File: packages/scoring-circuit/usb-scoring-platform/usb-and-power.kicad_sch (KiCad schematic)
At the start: 20 parts, among them J1 GCT USB4105-GF-A, U3 USBLC6-2SC6, U4 AP2112K-3.3TRG1, U5 Adafruit 5807 - set 20V, U6 D36V50F5, U7 AP63203WU-7

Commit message: feat(scoring-circuit): isolate computer USB in native KiCad draft
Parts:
- removed D1: SS14, Diode_SMD:D_SMA, symbol Diode:SS14
- removed R3, R4: 100k 1%, Resistor_SMD:R_0603_1608Metric, symbol Device:R
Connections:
- net GND: no longer C1.2, J1.A1 (GND), J1.A12 (GND), J1.B1 (GND), J1.B12 (GND), J1.SH (SHIELD), R1.2, R2.2, U3.2 (GND)
- net USB_DM renamed USB_HOST_DM
- net USB_DP renamed USB_HOST_DP
- new net USB_GND: C1.2, J1.A1 (GND), J1.A12 (GND), J1.B1 (GND), J1.B12 (GND), J1.SH (SHIELD), R1.2, R2.2, U3.2 (GND)
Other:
- note added: "Computer VBUS supplies only U3 and the upstream USB isolator. No direct USB-to-CORE power path or VBUS divider crosses the barrier."
- note added: "PD powers this revision. USB data is isolated on its own sheet. USB-only acquisition remains open: do not bridge USB_GND/VBUS into the board supply."
- note removed: "Computer USB powers acquisition only. Display, Ethernet and ESP32 require PD. Common-ground engineering draft; NOT an isolated fencing interface."

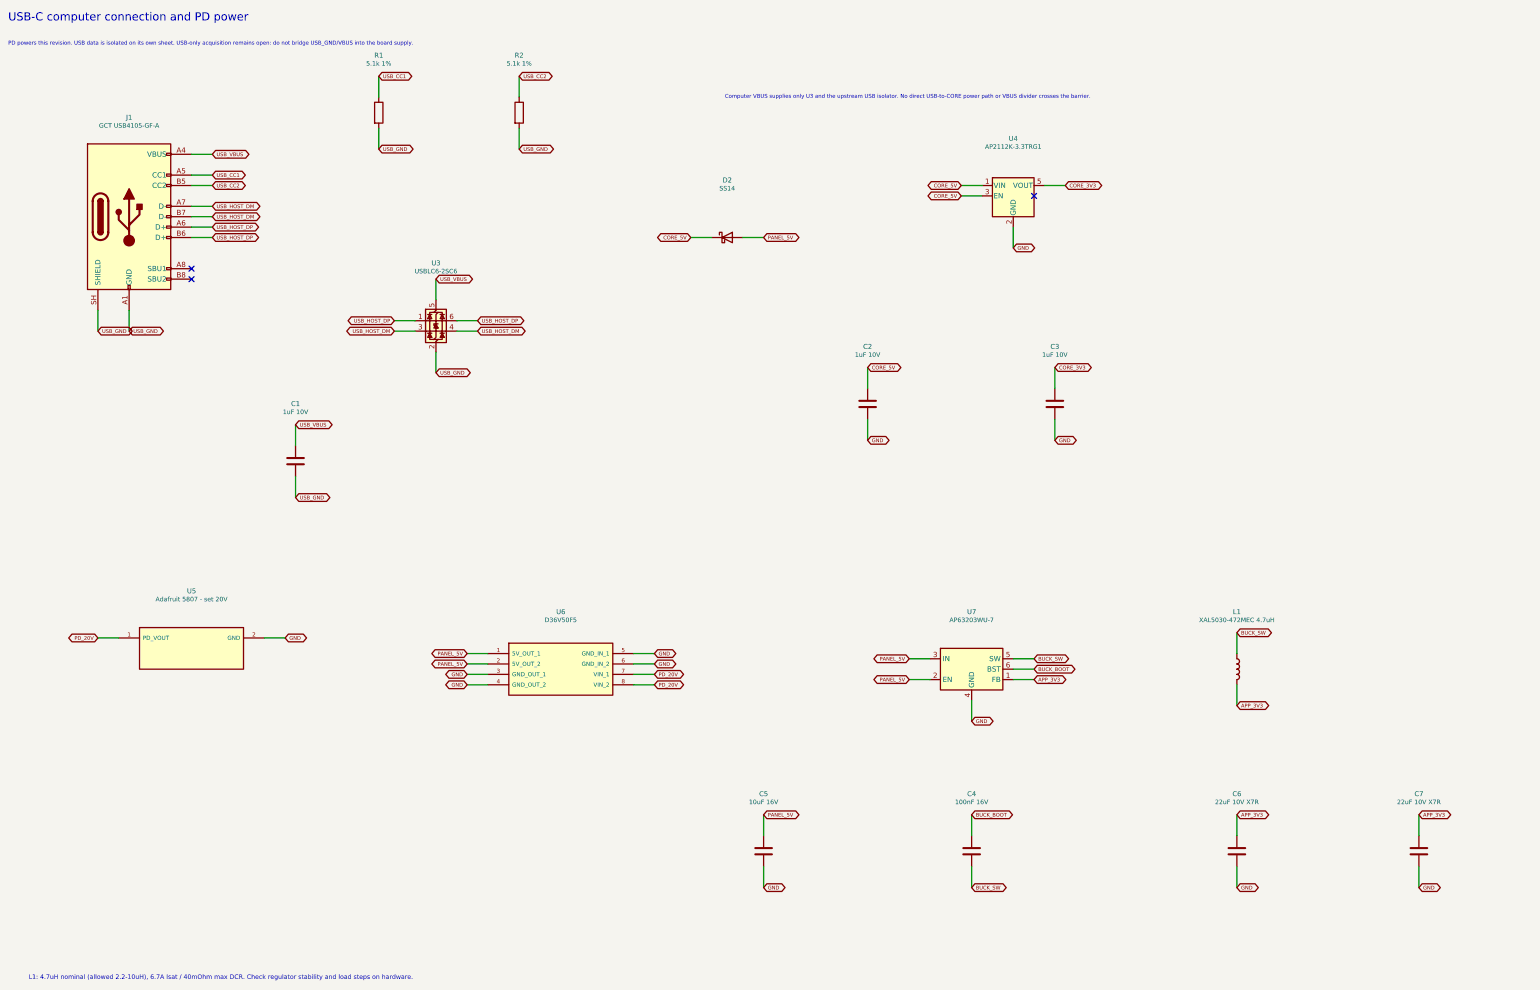
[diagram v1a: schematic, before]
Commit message: feat(scoring-circuit): add isolated single-cable USB acquisition power
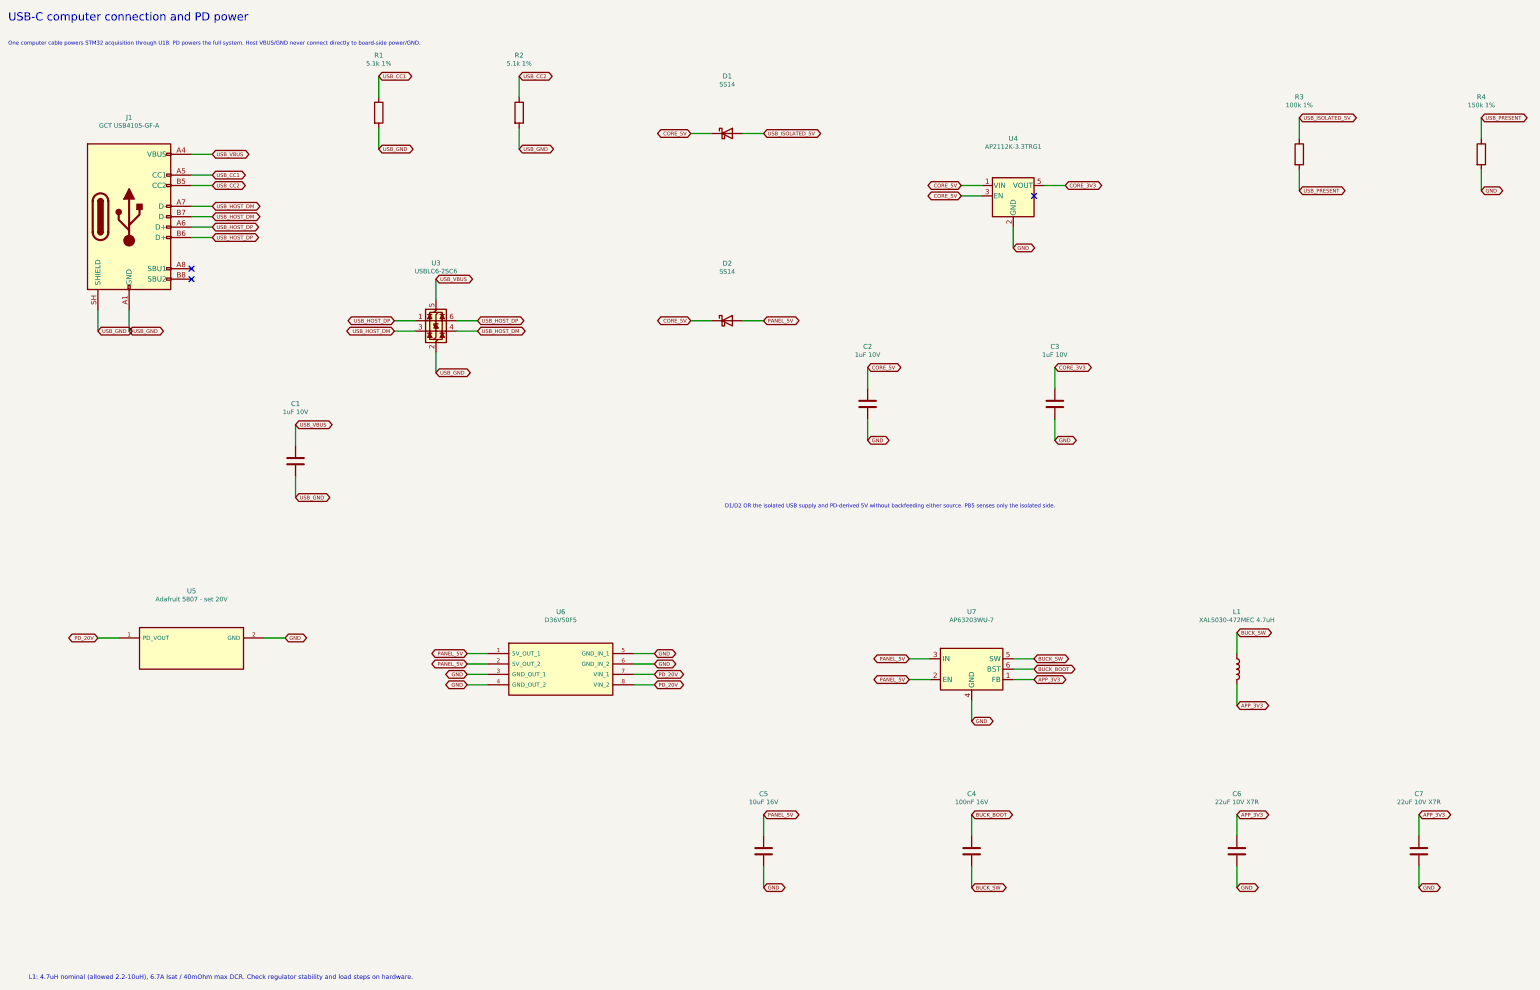
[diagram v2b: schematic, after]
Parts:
- added D1: SS14, Diode_SMD:D_SMA, symbol Diode:SS14
- added R3: 100k 1%, Resistor_SMD:R_0603_1608Metric, symbol Device:R
- added R4: 150k 1%, Resistor_SMD:R_0603_1608Metric, symbol Device:R
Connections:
- net CORE_5V: now also D1.1 (K)
- net GND: now also R4.2
- new net USB_ISOLATED_5V: D1.2 (A), R3.1
- new net USB_PRESENT: R3.2, R4.1
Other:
- note added: "D1/D2 OR the isolated USB supply and PD-derived 5V without backfeeding either source. PB5 senses only the isolated side."
- note added: "One computer cable powers STM32 acquisition through U18. PD powers the full system. Host VBUS/GND never connect directly to board-side power/GND."
- note removed: "Computer VBUS supplies only U3 and the upstream USB isolator. No direct USB-to-CORE power path or VBUS divider crosses the barrier."
- note removed: "PD powers this revision. USB data is isolated on its own sheet. USB-only acquisition remains open: do not bridge USB_GND/VBUS into the board supply."
- moved on the sheet: D2

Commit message: feat(scoring-circuit): decouple USB data protection from VBUS
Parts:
- C1: value 1uF 10V -> 1uF 50V
- U3: value USBLC6-2SC6 -> TPD2E2U06DCKR; footprint Package_TO_SOT_SMD:SOT-23-6 -> ScoringPlatform:TPD2E2U06DCKR; symbol Power_Protection:USBLC6-2SC6 -> Power_Protection:TPD2E2U06DCK
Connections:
- net USB_GND: now also U3.3; no longer U3.2 (GND)
- net USB_HOST_DM: now also U3.2; no longer U3.3 (I/O2), U3.4 (I/O2)
- net USB_HOST_DP: no longer U3.6 (I/O1)
- net USB_VBUS: no longer U3.5 (VBUS)
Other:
- note added: "U3: supply-independent D+/D- protection; no VBUS clamp pin. C1: 50V rating for planned shared PD input. U18 still requires protected input <=16.5V; shared USB-C power conversion remains unfinished."

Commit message: feat(scoring-circuit): replace dual USB inputs with shared isolated power design
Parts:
- removed R1, R2: 5.1k 1%, Resistor_SMD:R_0603_1608Metric, symbol Device:R
- removed U5: Adafruit 5807 - set 20V, ScoringPlatform:Adafruit_5807, symbol ScoringPlatform:Adafruit_5807
- removed U6: D36V50F5, ScoringPlatform:Pololu_D36V50F5, symbol ScoringPlatform:Pololu_D36V50F5
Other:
- note added: "J1 is the only USB-C receptacle. Shared power conversion and PD control are on usb-pd-power. D+/D- remain isolated by U18."
- note removed: "U3: supply-independent D+/D- protection; no VBUS clamp pin. C1: 50V rating for planned shared PD input. U18 still requires protected input <=16.5V; shared USB-C power conversion remains unfinished."
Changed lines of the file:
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@@
 (wire (pts (xy 41.91 87.63) (xy 41.91 92.71)) (stroke (width 0) (type default)))
 (global_label "USB_GND" (shape bidirectional) (at 41.91 92.71 0) (effects (font (size 0.9 0.9)) (justify left)) (property "Intersheetrefs" "" (at 41.91 92.71 0) (effects (font (size 1 1)) (hide yes))))
-(symbol (lib_id "Device:R") (at 110.49 39.37 0) (unit 1) (in_bom yes) (on_board yes) (dnp no) (property "Reference" "R1" (at 110.49 25.37 0) (effects (font (size 1.2 1.2)))) (property "Value" "5.1k 1%" (at 110.49 27.37 0) (effects (font (size 1.1 1.1)))) (property "Footprint" "Resistor_SMD:R_0603_1608Metric" (at 110.49 39.37 0) (effects (font (size 1 1)) (hide yes))) (pin "1") (pin "2") (instances (project "usb-scoring-platform" (path "/20cc8167-128c-446a-a106-f942323e143f/36d13c9b-c278-4925-a3f2-4480b5a41043" (reference "R1") (unit 1)))))
-(wire (pts (xy 110.49 35.56) (xy 110.49 30.48)) (stroke (width 0) (type default)))
-(global_label "USB_CC1" (shape bidirectional) (at 110.49 30.48 0) (effects (font (size 0.9 0.9)) (justify left)) (property "Intersheetrefs" "" (at 110.49 30.48 0) (effects (font (size 1 1)) (hide yes))))
-(wire (pts (xy 110.49 43.18) (xy 110.49 48.26)) (stroke (width 0) (type default)))
-(global_label "USB_GND" (shape bidirectional) (at 110.49 48.26 0) (effects (font (size 0.9 0.9)) (justify left)) (property "Intersheetrefs" "" (at 110.49 48.26 0) (effects (font (size 1 1)) (hide yes))))
-(symbol (lib_id "Device:R") (at 144.78 39.37 0) (unit 1) (in_bom yes) (on_board yes) (dnp no) (property "Reference" "R2" (at 144.78 25.37 0) (effects (font (size 1.2 1.2)))) (property "Value" "5.1k 1%" (at 144.78 27.37 0) (effects (font (size 1.1 1.1)))) (property "Footprint" "Resistor_SMD:R_0603_1608Metric" (at 144.78 39.37 0) (effects (font (size 1 1)) (hide yes))) (pin "1") (pin "2") (instances (project "usb-scoring-platform" (path "/20cc8167-128c-446a-a106-f942323e143f/36d13c9b-c278-4925-a3f2-4480b5a41043" (reference "R2") (unit 1)))))
-(wire (pts (xy 144.78 35.56) (xy 144.78 30.48)) (stroke (width 0) (type default)))
-(global_label "USB_CC2" (shape bidirectional) (at 144.78 30.48 0) (effects (font (size 0.9 0.9)) (justify left)) (property "Intersheetrefs" "" (at 144.78 30.48 0) (effects (font (size 1 1)) (hide yes))))
-(wire (pts (xy 144.78 43.18) (xy 144.78 48.26)) (stroke (width 0) (type default)))
-(global_label "USB_GND" (shape bidirectional) (at 144.78 48.26 0) (effects (font (size 0.9 0.9)) (justify left)) (property "Intersheetrefs" "" (at 144.78 48.26 0) (effects (font (size 1 1)) (hide yes))))
 (symbol (lib_id "Power_Protection:TPD2E2U06DCK") (at 124.46 90.17 0) (unit 1) (in_bom yes) (on_board yes) (dnp no) (property "Reference" "U3" (at 124.46 76.09 0) (effects (font (size 1.2 1.2)))) (property "Value" "TPD2E2U06DCKR" (at 124.46 78.09 0) (effects (font (size 1.1 1.1)))) (property "Footprint" "ScoringPlatform:TPD2E2U06DCKR" (at 124.46 90.17 0) (effects (font (size 1 1)) (hide yes))) (instances (project "usb-scoring-platform" (path "/20cc8167-128c-446a-a106-f942323e143f/36d13c9b-c278-4925-a3f2-4480b5a41043" (reference "U3") (unit 1)))) (property "Datasheet" "https://www.ti.com/lit/ds/symlink/tpd2e2u06.pdf" (at 124.46 90.17 0) (effects (font (size 1 1)) (hide yes))) (pin "1") (pin "2") (pin "3"))
 (symbol (lib_id "Device:C") (at 90.17 124.46 0) (unit 1) (in_bom yes) (on_board yes) (dnp no) (property "Reference" "C1" (at 90.17 110.46 0) (effects (font (size 1.2 1.2)))) (property "Value" "1uF 50V" (at 90.17 112.46 0) (effects (font (size 1.1 1.1)))) (property "Footprint" "Capacitor_SMD:C_0603_1608Metric" (at 90.17 124.46 0) (effects (font (size 1 1)) (hide yes))) (pin "1") (pin "2") (instances (project "usb-scoring-platform" (path "/20cc8167-128c-446a-a106-f942323e143f/36d13c9b-c278-4925-a3f2-4480b5a41043" (reference "C1") (unit 1)))))
@@
 (global_label "GND" (shape bidirectional) (at 379.73 58.42 0) (effects (font (size 0.9 0.9)) (justify left)) (property "Intersheetrefs" "" (at 379.73 58.42 0) (effects (font (size 1 1)) (hide yes))))
 (text "D1/D2 OR the isolated USB supply and PD-derived 5V without backfeeding either source. PB5 senses only the isolated side." (at 195 135 0) (effects (font (size 0.95 0.95)) (justify left top)))
-(symbol (lib_id "ScoringPlatform:Adafruit_5807") (at 64.77 170.18 0) (unit 1) (in_bom yes) (on_board yes) (dnp no) (property "Reference" "U5" (at 64.77 156.18 0) (effects (font (size 1.2 1.2)))) (property "Value" "Adafruit 5807 - set 20V" (at 64.77 158.18 0) (effects (font (size 1.1 1.1)))) (property "Footprint" "ScoringPlatform:Adafruit_5807" (at 64.77 170.18 0) (effects (font (size 1 1)) (hide yes))) (pin "1") (pin "2") (instances (project "usb-scoring-platform" (path "/20cc8167-128c-446a-a106-f942323e143f/36d13c9b-c278-4925-a3f2-4480b5a41043" (reference "U5") (unit 1)))))
-(wire (pts (xy 46.99 167.64) (xy 41.91 167.64)) (stroke (width 0) (type default)))
-(global_label "PD_20V" (shape bidirectional) (at 41.91 167.64 180) (effects (font (size 0.9 0.9)) (justify right)) (property "Intersheetrefs" "" (at 41.91 167.64 180) (effects (font (size 1 1)) (hide yes))))
-(wire (pts (xy 82.55 167.64) (xy 87.63 167.64)) (stroke (width 0) (type default)))
-(global_label "GND" (shape bidirectional) (at 87.63 167.64 0) (effects (font (size 0.9 0.9)) (justify left)) (property "Intersheetrefs" "" (at 87.63 167.64 0) (effects (font (size 1 1)) (hide yes))))
-(symbol (lib_id "ScoringPlatform:Pololu_D36V50F5") (at 154.94 175.26 0) (unit 1) (in_bom yes) (on_board yes) (dnp no) (property "Reference" "U6" (at 154.94 161.26 0) (effects (font (size 1.2 1.2)))) (property "Value" "D36V50F5" (at 154.94 163.26 0) (effects (font (size 1.1 1.1)))) (property "Footprint" "ScoringPlatform:Pololu_D36V50F5" (at 154.94 175.26 0) (effects (font (size 1 1)) (hide yes))) (pin "1") (pin "2") (pin "3") (pin "4") (pin "5") (pin "6") (pin "7") (pin "8") (instances (project "usb-scoring-platform" (path "/20cc8167-128c-446a-a106-f942323e143f/36d13c9b-c278-4925-a3f2-4480b5a41043" (reference "U6") (unit 1)))))
-(wire (pts (xy 137.16 171.45) (xy 132.08 171.45)) (stroke (width 0) (type default)))
-(global_label "PANEL_5V" (shape bidirectional) (at 132.08 171.45 180) (effects (font (size 0.9 0.9)) (justify right)) (property "Intersheetrefs" "" (at 132.08 171.45 180) (effects (font (size 1 1)) (hide yes))))
-(wire (pts (xy 137.16 173.99) (xy 132.08 173.99)) (stroke (width 0) (type default)))
-(global_label "PANEL_5V" (shape bidirectional) (at 132.08 173.99 180) (effects (font (size 0.9 0.9)) (justify right)) (property "Intersheetrefs" "" (at 132.08 173.99 180) (effects (font (size 1 1)) (hide yes))))
-(wire (pts (xy 137.16 176.53) (xy 132.08 176.53)) (stroke (width 0) (type default)))
-(global_label "GND" (shape bidirectional) (at 132.08 176.53 180) (effects (font (size 0.9 0.9)) (justify right)) (property "Intersheetrefs" "" (at 132.08 176.53 180) (effects (font (size 1 1)) (hide yes))))
-(wire (pts (xy 137.16 179.07) (xy 132.08 179.07)) (stroke (width 0) (type default)))
-(global_label "GND" (shape bidirectional) (at 132.08 179.07 180) (effects (font (size 0.9 0.9)) (justify right)) (property "Intersheetrefs" "" (at 132.08 179.07 180) (effects (font (size 1 1)) (hide yes))))
-(wire (pts (xy 172.72 171.45) (xy 177.8 171.45)) (stroke (width 0) (type default)))
-(global_label "GND" (shape bidirectional) (at 177.8 171.45 0) (effects (font (size 0.9 0.9)) (justify left)) (property "Intersheetrefs" "" (at 177.8 171.45 0) (effects (font (size 1 1)) (hide yes))))
-(wire (pts (xy 172.72 173.99) (xy 177.8 173.99)) (stroke (width 0) (type default)))
-(global_label "GND" (shape bidirectional) (at 177.8 173.99 0) (effects (font (size 0.9 0.9)) (justify left)) (property "Intersheetrefs" "" (at 177.8 173.99 0) (effects (font (size 1 1)) (hide yes))))
-(wire (pts (xy 172.72 176.53) (xy 177.8 176.53)) (stroke (width 0) (type default)))
-(global_label "PD_20V" (shape bidirectional) (at 177.8 176.53 0) (effects (font (size 0.9 0.9)) (justify left)) (property "Intersheetrefs" "" (at 177.8 176.53 0) (effects (font (size 1 1)) (hide yes))))
-(wire (pts (xy 172.72 179.07) (xy 177.8 179.07)) (stroke (width 0) (type default)))
-(global_label "PD_20V" (shape bidirectional) (at 177.8 179.07 0) (effects (font (size 0.9 0.9)) (justify left)) (property "Intersheetrefs" "" (at 177.8 179.07 0) (effects (font (size 1 1)) (hide yes))))
 (symbol (lib_id "Regulator_Switching:AP63203WU") (at 255.27 175.26 0) (unit 1) (in_bom yes) (on_board yes) (dnp no) (property "Reference" "U7" (at 255.27 161.26 0) (effects (font (size 1.2 1.2)))) (property "Value" "AP63203WU-7" (at 255.27 163.26 0) (effects (font (size 1.1 1.1)))) (property "Footprint" "Package_TO_SOT_SMD:TSOT-23-6" (at 255.27 175.26 0) (effects (font (size 1 1)) (hide yes))) (pin "1") (pin "2") (pin "3") (pin "4") (pin "5") (pin "6") (instances (project "usb-scoring-platform" (path "/20cc8167-128c-446a-a106-f942323e143f/36d13c9b-c278-4925-a3f2-4480b5a41043" (reference "U7") (unit 1)))))
 (wire (pts (xy 265.43 177.8) (xy 270.51 177.8)) (stroke (width 0) (type default)))
@@
 (wire (pts (xy 124.46 97.79) (xy 124.46 102.87)) (stroke (width 0) (type default)))
 (global_label "USB_GND" (shape bidirectional) (at 124.46 102.87 0) (effects (font (size .9 .9)) (justify left)) (property "Intersheetrefs" "" (at 124.46 102.87 0) (effects (font (size 1 1)) (hide yes))))
-(text "U3: supply-independent D+/D- protection; no VBUS clamp pin. C1: 50V rating for planned shared PD input. U18 still requires protected input <=16.5V; shared USB-C power conversion remains unfinished." (at 20.32 210.82 0) (effects (font (size 1.1 1.1)) (justify left top))))
+(text "J1 is the only USB-C receptacle. Shared power conversion and PD control are on usb-pd-power. D+/D- remain isolated by U18." (at 20.32 210.82 0) (effects (font (size 1.1 1.1)) (justify left top))))

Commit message: feat(scoring-circuit): specify USB input bypass capacitor
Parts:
- C1: MPN (none) -> C1608X7R1H105K080AB; Manufacturer (none) -> TDK
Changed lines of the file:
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@@
 (global_label "USB_GND" (shape bidirectional) (at 41.91 92.71 0) (effects (font (size 0.9 0.9)) (justify left)) (property "Intersheetrefs" "" (at 41.91 92.71 0) (effects (font (size 1 1)) (hide yes))))
 (symbol (lib_id "Power_Protection:TPD2E2U06DCK") (at 124.46 90.17 0) (unit 1) (in_bom yes) (on_board yes) (dnp no) (property "Reference" "U3" (at 124.46 76.09 0) (effects (font (size 1.2 1.2)))) (property "Value" "TPD2E2U06DCKR" (at 124.46 78.09 0) (effects (font (size 1.1 1.1)))) (property "Footprint" "ScoringPlatform:TPD2E2U06DCKR" (at 124.46 90.17 0) (effects (font (size 1 1)) (hide yes))) (instances (project "usb-scoring-platform" (path "/20cc8167-128c-446a-a106-f942323e143f/36d13c9b-c278-4925-a3f2-4480b5a41043" (reference "U3") (unit 1)))) (property "Datasheet" "https://www.ti.com/lit/ds/symlink/tpd2e2u06.pdf" (at 124.46 90.17 0) (effects (font (size 1 1)) (hide yes))) (pin "1") (pin "2") (pin "3"))
-(symbol (lib_id "Device:C") (at 90.17 124.46 0) (unit 1) (in_bom yes) (on_board yes) (dnp no) (property "Reference" "C1" (at 90.17 110.46 0) (effects (font (size 1.2 1.2)))) (property "Value" "1uF 50V" (at 90.17 112.46 0) (effects (font (size 1.1 1.1)))) (property "Footprint" "Capacitor_SMD:C_0603_1608Metric" (at 90.17 124.46 0) (effects (font (size 1 1)) (hide yes))) (pin "1") (pin "2") (instances (project "usb-scoring-platform" (path "/20cc8167-128c-446a-a106-f942323e143f/36d13c9b-c278-4925-a3f2-4480b5a41043" (reference "C1") (unit 1)))))
+(symbol (lib_id "Device:C") (at 90.17 124.46 0) (unit 1) (in_bom yes) (on_board yes) (dnp no) (property "Reference" "C1" (at 90.17 110.46 0) (effects (font (size 1.2 1.2)))) (property "Value" "1uF 50V" (at 90.17 112.46 0) (effects (font (size 1.1 1.1)))) (property "Footprint" "Capacitor_SMD:C_0603_1608Metric" (at 90.17 124.46 0) (effects (font (size 1 1)) (hide yes))) (property "Manufacturer" "TDK" (at 90.17 124.46 0) (effects (font (size 1 1)) (hide yes))) (property "MPN" "C1608X7R1H105K080AB" (at 90.17 124.46 0) (effects (font (size 1 1)) (hide yes))) (property "Datasheet" "https://product.tdk.com/en/search/capacitor/ceramic/mlcc/info?part_no=C1608X7R1H105K080AB" (at 90.17 124.46 0) (effects (font (size 1 1)) (hide yes))) (pin "1") (pin "2") (instances (project "usb-scoring-platform" (path "/20cc8167-128c-446a-a106-f942323e143f/36d13c9b-c278-4925-a3f2-4480b5a41043" (reference "C1") (unit 1)))))
 (wire (pts (xy 90.17 120.65) (xy 90.17 115.57)) (stroke (width 0) (type default)))
 (global_label "USB_VBUS" (shape bidirectional) (at 90.17 115.57 0) (effects (font (size 0.9 0.9)) (justify left)) (property "Intersheetrefs" "" (at 90.17 115.57 0) (effects (font (size 1 1)) (hide yes))))
